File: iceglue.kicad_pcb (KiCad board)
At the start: 2 copper layers, 23.6 x 57.7 mm, 36 parts, among them J1 USB_OTG, J2 TEST_1P, J3 Conn_01x22, J4 Conn_01x22, J5 TEST_1P, J6 TEST_1P, SW1 SW_Push, U1 STM32F070F6P6, U2 ICE40UP5K-SG48, U3 LD1117S33TR_SOT223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

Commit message: add crystal and usb esd; crystal has to be somwhere else
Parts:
- added C18: 22p, Capacitors_SMD:C_0603_HandSoldering, B.Cu at (161.5, 124.5)
- added C19: 22p, Capacitors_SMD:C_0603_HandSoldering, B.Cu at (165.8, 113.4)
- added DZ1: USBLC6-2SC6, TO_SOT_Packages_SMD:SOT-23-6_Handsoldering, F.Cu at (158.6, 113.3)
- added FID1: FIDUCIAL, Fiducials:Fiducial_classic_Small_CopperBottom_Type1, F.Cu at (186.4, 173.7)
- added FID2: FIDUCIAL, Fiducials:Fiducial_classic_Small_CopperBottom_Type1, F.Cu at (200.7, 156.5)
- added FID3: FIDUCIAL, Fiducials:Fiducial_classic_Small_CopperTop_Type1, F.Cu at (182.1, 158.2)
- added FID4: FIDUCIAL, Fiducials:Fiducial_classic_Small_CopperTop_Type1, F.Cu at (138.7, 168.7)
- added J7: TEST_1P, Measurement_Points:Measurement_Point_Round-SMD-Pad_Small, B.Cu at (165.7, 108.3)
- added J8: TEST_1P, Measurement_Points:Measurement_Point_Round-SMD-Pad_Small, B.Cu at (165.8, 110.9)
- added Y1: 8MHz, kicad-libraries:HC49%2fUS, B.Cu at (165.1, 121.8)
- C2: moved to B.Cu
- moved C2 4.30 mm to (155.4, 115.1), turned to 270 degrees
- moved J2 2.01 mm to (154.1, 117.8)
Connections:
- J1 pad 2: /USB_D- -> Net-(DZ1-Pad1)
- J1 pad 3: /USB_D+ -> Net-(DZ1-Pad3)
- U1 pad 10: (no net) -> /RESET
- U1 pad 19: (no net) -> Net-(J8-Pad1)
- U1 pad 2: (no net) -> Net-(C18-Pad2)
- U1 pad 20: /RESET -> Net-(J7-Pad1)
- U1 pad 3: (no net) -> Net-(C19-Pad1)
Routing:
- net GND: track 244.2 -> 275.4 mm, vias 8 -> 7
- net Net-(C18-Pad2): track 0.00 -> 20.5 mm
- net Net-(C19-Pad1): track 0.00 -> 9.16 mm
- net Net-(J8-Pad1): track 0.00 -> 4.88 mm
- net Net-(DZ1-Pad3): track 0.00 -> 4.49 mm
- net /USB_D-: track 3.28 -> 7.48 mm
- net Net-(J7-Pad1): track 0.00 -> 3.79 mm
- net /RESET: track 48.0 -> 51.7 mm, vias 3 -> 1
- net /USB_D+: track 6.05 -> 9.02 mm
- net Net-(DZ1-Pad1): track 0.00 -> 2.91 mm
- net /SPI_SCK: track 50.9 -> 48.1 mm
- net +3V3: track 117.4 -> 120.2 mm, vias 7 -> 6
- net +5V: track 155.7 -> 158.2 mm
- net /SPI_MISO: track 52.7 -> 53.8 mm
- net /SPI_MOSI: track 48.6 -> 49.5 mm
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
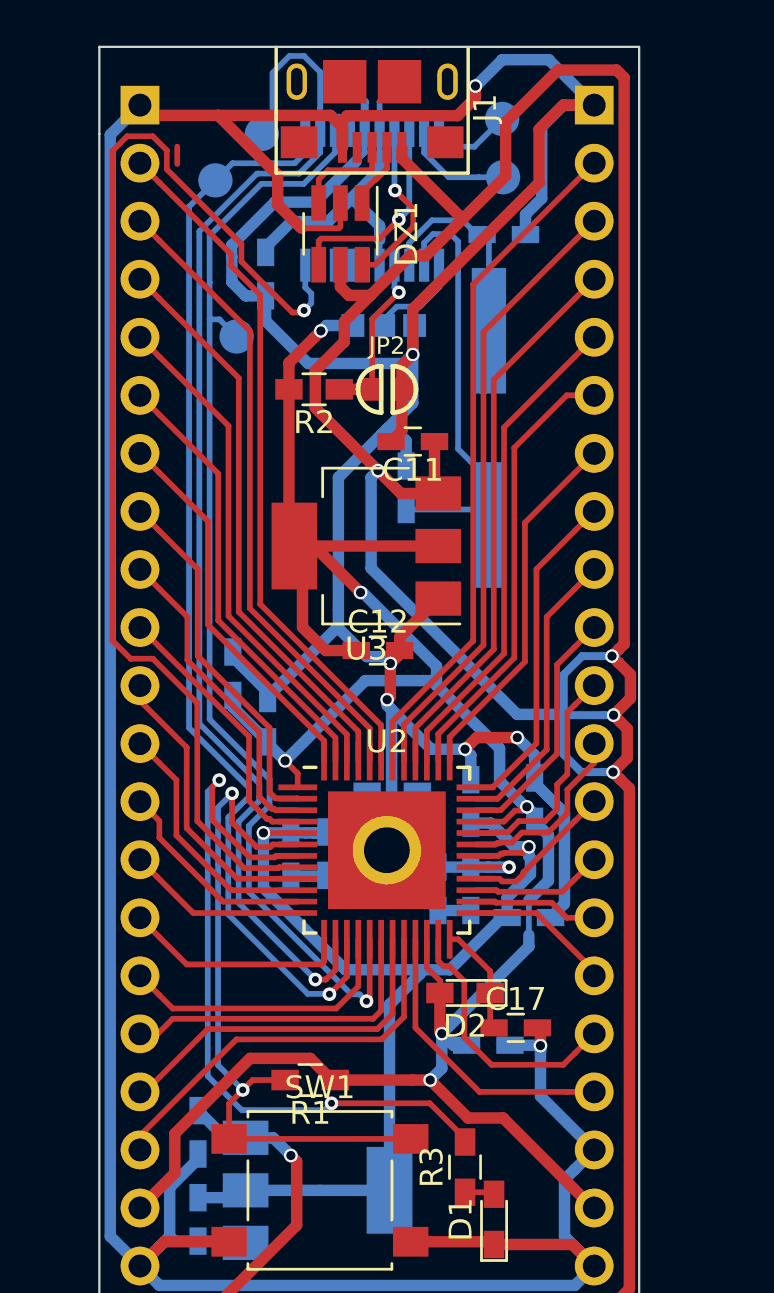
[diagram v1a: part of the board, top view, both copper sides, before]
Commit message: move crystal to be not _that_ bad
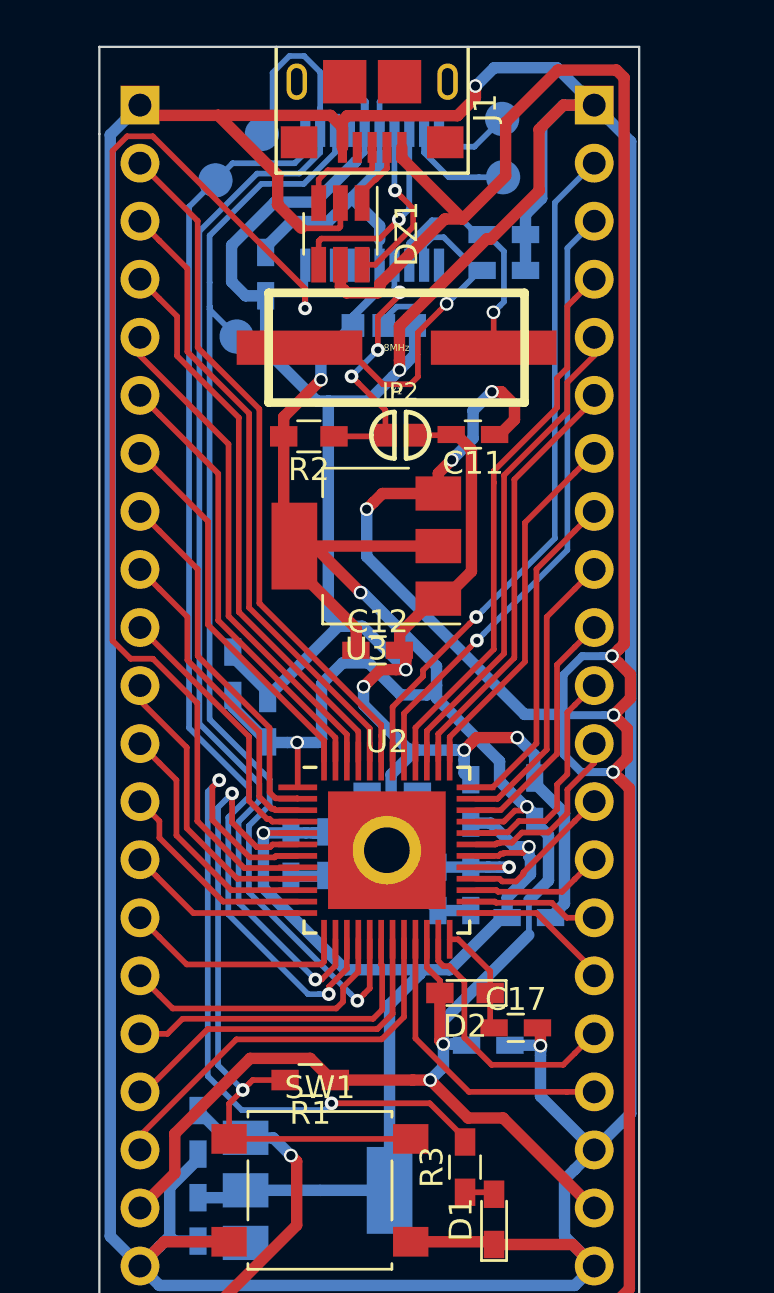
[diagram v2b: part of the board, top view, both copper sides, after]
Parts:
- Y1: moved to F.Cu
- moved C18 10.4 mm to (165.8, 114.9), turned to 180 degrees
- moved Y1 5.35 mm to (161.1, 118.3), turned to 180 degrees
- moved C11 2.65 mm to (164.4, 122.1)
- moved JP2 2.09 mm to (161.2, 122.2)
- moved R2 2.07 mm to (157.2, 122.2)
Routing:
- net GND: track 275.4 -> 329.4 mm
- net +5V: track 158.2 -> 153.3 mm, vias 5 -> 7
- net Net-(C18-Pad2): track 20.5 -> 15.8 mm, vias 0 -> 1
- net Net-(JP2-Pad2): track 7.44 -> 11.3 mm, vias 1 -> 3
- net +3V3: track 120.2 -> 121.6 mm
- net Net-(C19-Pad1): track 9.16 -> 10.5 mm, vias 0 -> 1
- net /RESET: track 51.7 -> 50.9 mm
- net (no net): track 0.76 -> 0.00 mm
- net /IO_30: track 19.5 -> 18.8 mm
- net /IO_34: vias 0 -> 1
- net /IO_33: vias 0 -> 1

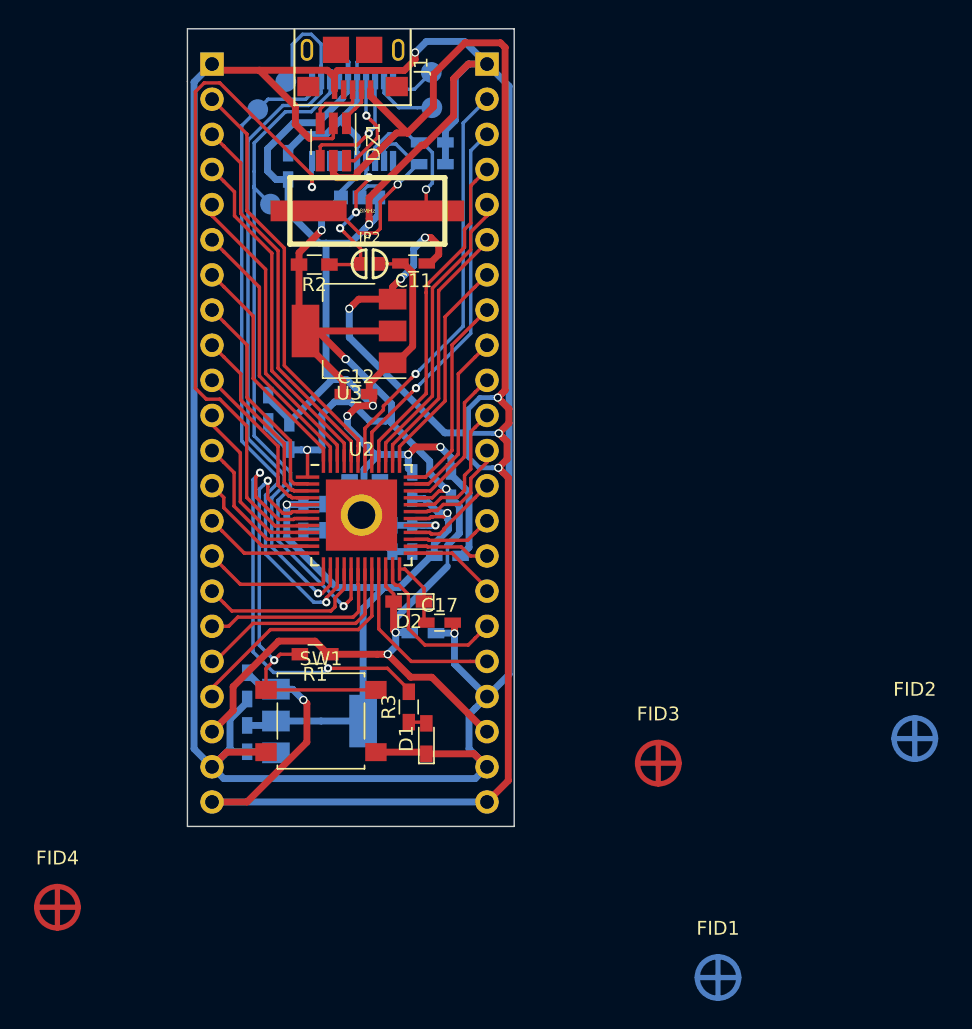
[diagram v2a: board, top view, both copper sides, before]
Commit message: add silkscreen layout + logos; closes #1
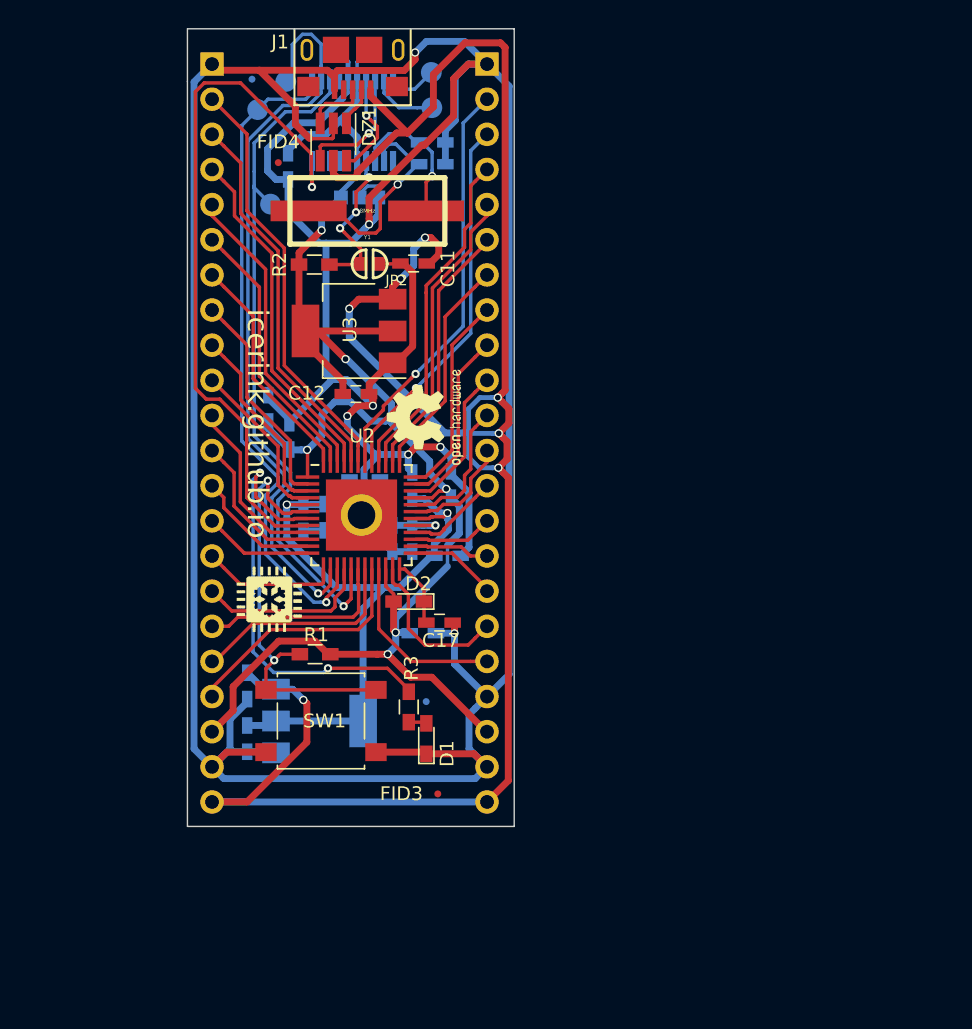
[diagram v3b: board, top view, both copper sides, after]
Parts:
- added G***: LOGO, OPENHARDWARE:OSHWLOGO0.3IN, F.Cu at (161.6, 137.1)
- added LOGO: , lib:logo, F.Cu at (156.5, 148.9)
- FID1, FID2: footprint Fiducials:Fiducial_classic_Small_CopperBottom_Type1 -> Fiducials:Fiducial_0.5mm_Dia_1mm_Outer; moved to B.Cu
- FID3, FID4: footprint Fiducials:Fiducial_classic_Small_CopperTop_Type1 -> Fiducials:Fiducial_0.5mm_Dia_1mm_Outer
- moved FID1 73.2 mm to (152.8, 108.8)
- moved FID4 56.1 mm to (154.7, 114.8)
- moved FID2 35.4 mm to (165.3, 153.8)
- moved FID3 16.1 mm to (166.2, 160.5)
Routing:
- net /RESET: track 50.9 -> 51.8 mm
- net +3V3: track 121.6 -> 121.1 mm
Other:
- board text added: "icerink.github.io"

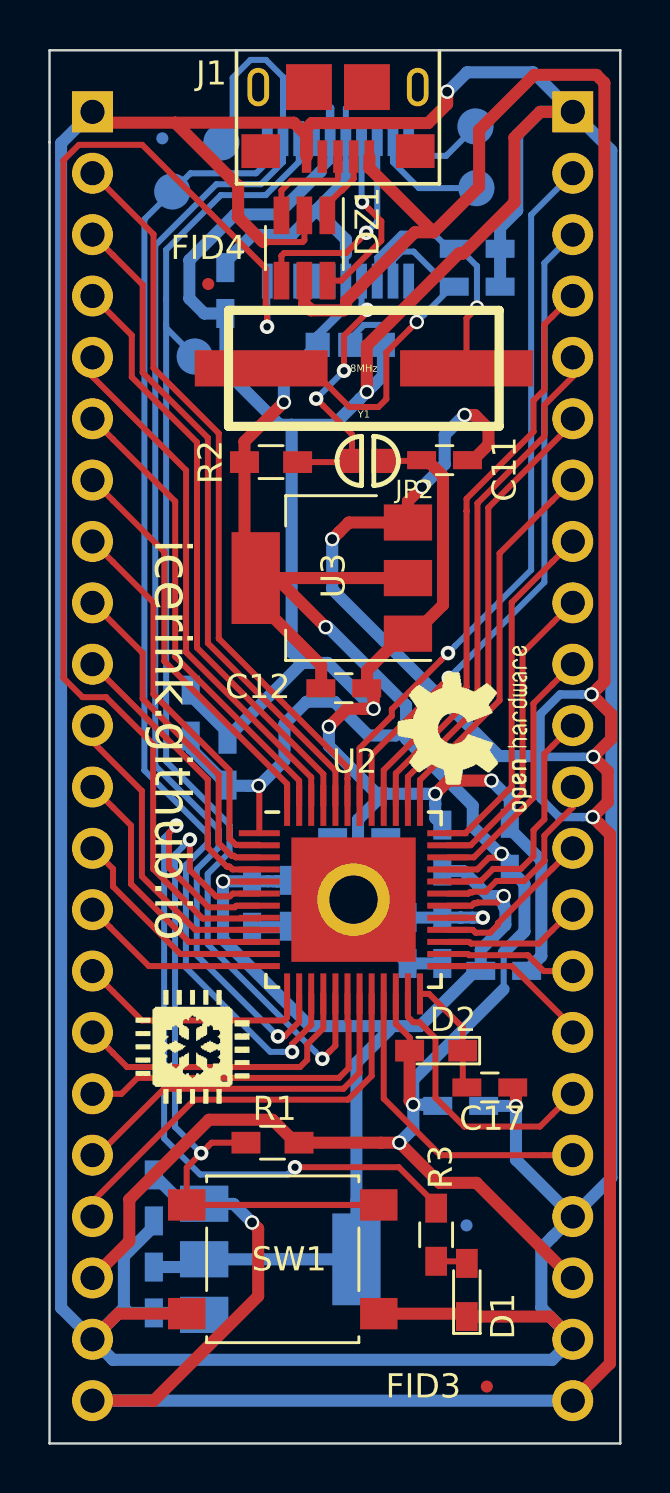
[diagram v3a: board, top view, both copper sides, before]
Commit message: add io labels; optimize silkscreen
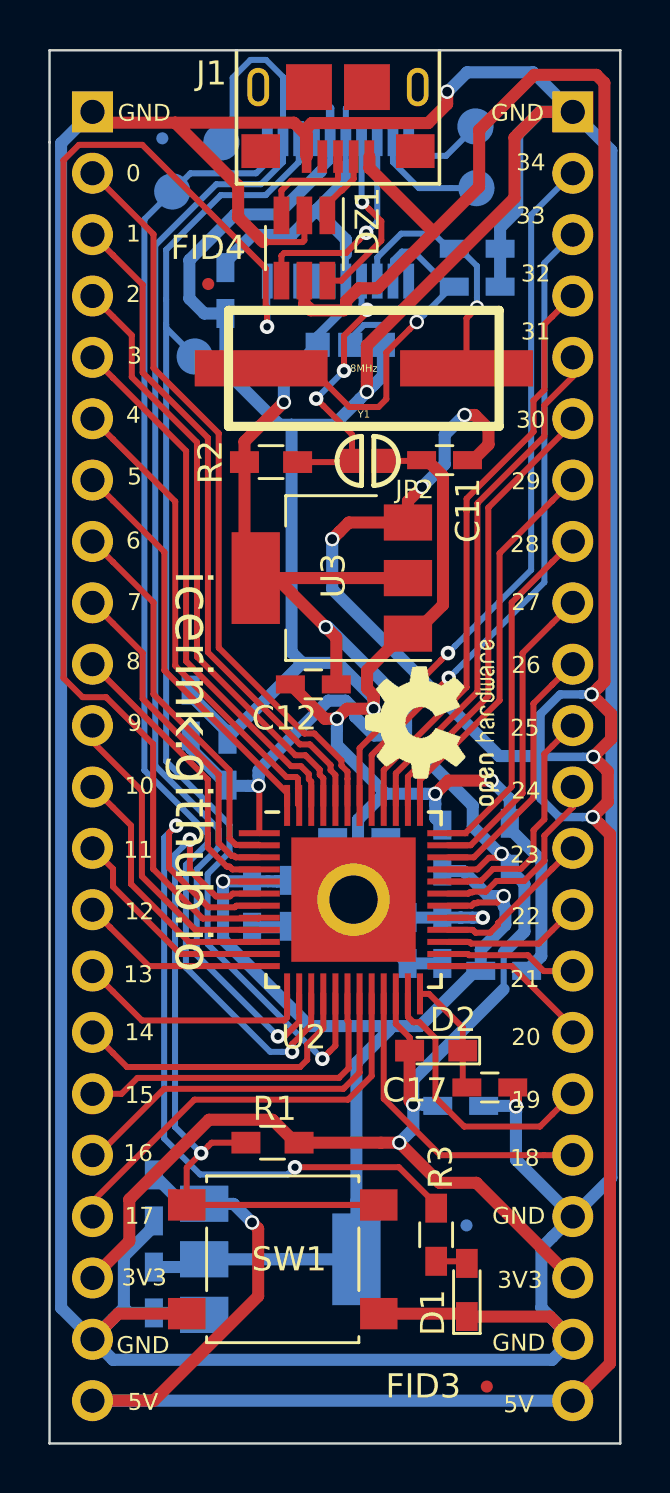
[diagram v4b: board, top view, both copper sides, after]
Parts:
- LOGO: moved to B.Cu
- moved LOGO 28.2 mm to (162.6, 121.4)
- moved G*** 1.37 mm to (160.2, 136.8)
- moved C12 1.27 mm to (159.0, 131.4), turned to 180 degrees
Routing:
- net +3V3: track 121.1 -> 117.7 mm
- net GND: track 329.4 -> 331.6 mm
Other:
- board text added: "0"
- board text added: "1"
- board text added: "10"
- board text added: "11"
- board text added: "12"
- board text added: "13"
- board text added: "14"
- board text added: "15"
- board text added: "16"
- board text added: "17"
- board text added: "18"
- board text added: "19"
- board text added: "2"
- board text added: "20"
- board text added: "21"
- board text added: "22"
- board text added: "23"
- board text added: "24"
- board text added: "25"
- board text added: "26"
- board text added: "27"
- board text added: "28"
- board text added: "29"
- board text added: "3"
- board text added: "30"
- board text added: "31"
- board text added: "32"
- board text added: "33"
- board text added: "34"
- board text added: "3V3"
- board text added: "4"
- board text added: "5"
- board text added: "5V"
- board text added: "6"
- board text added: "7"
- board text added: "8"
- board text added: "9"
- board text added: "GND"
- board text added: "iceskate 1.0"
